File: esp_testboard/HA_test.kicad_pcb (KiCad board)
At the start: 2 copper layers, 8.3 x 5.1 mm, 90 parts, among them J1 ESP-01, J10 ESP-01, J11 SHT21, J12 SHT21, J13 SHT21, J14 SHT21, J15 SHT21, J16 PWR_IN, J17 PWR_USB, J18 UART, J2 ESP-01, J3 ESP-01, J4 ESP-01, J5 ESP-01, J6 ESP-01, J7 ESP-01, J8 ESP-01, J9 ESP-01, U1 AMS1117-3.3, U2 AMS1117-3.3

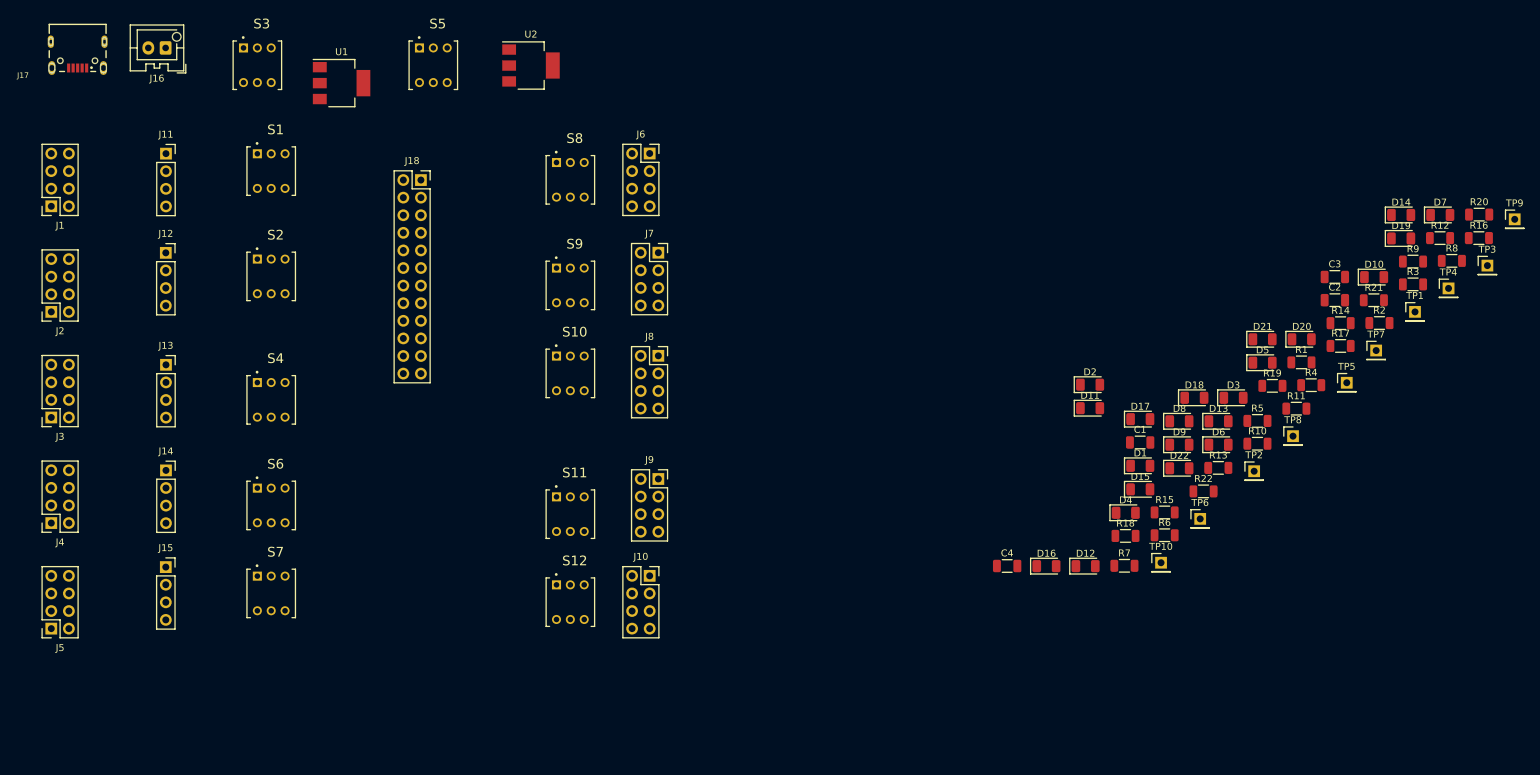
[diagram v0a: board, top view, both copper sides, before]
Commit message: schematic and PCB for ESP tester
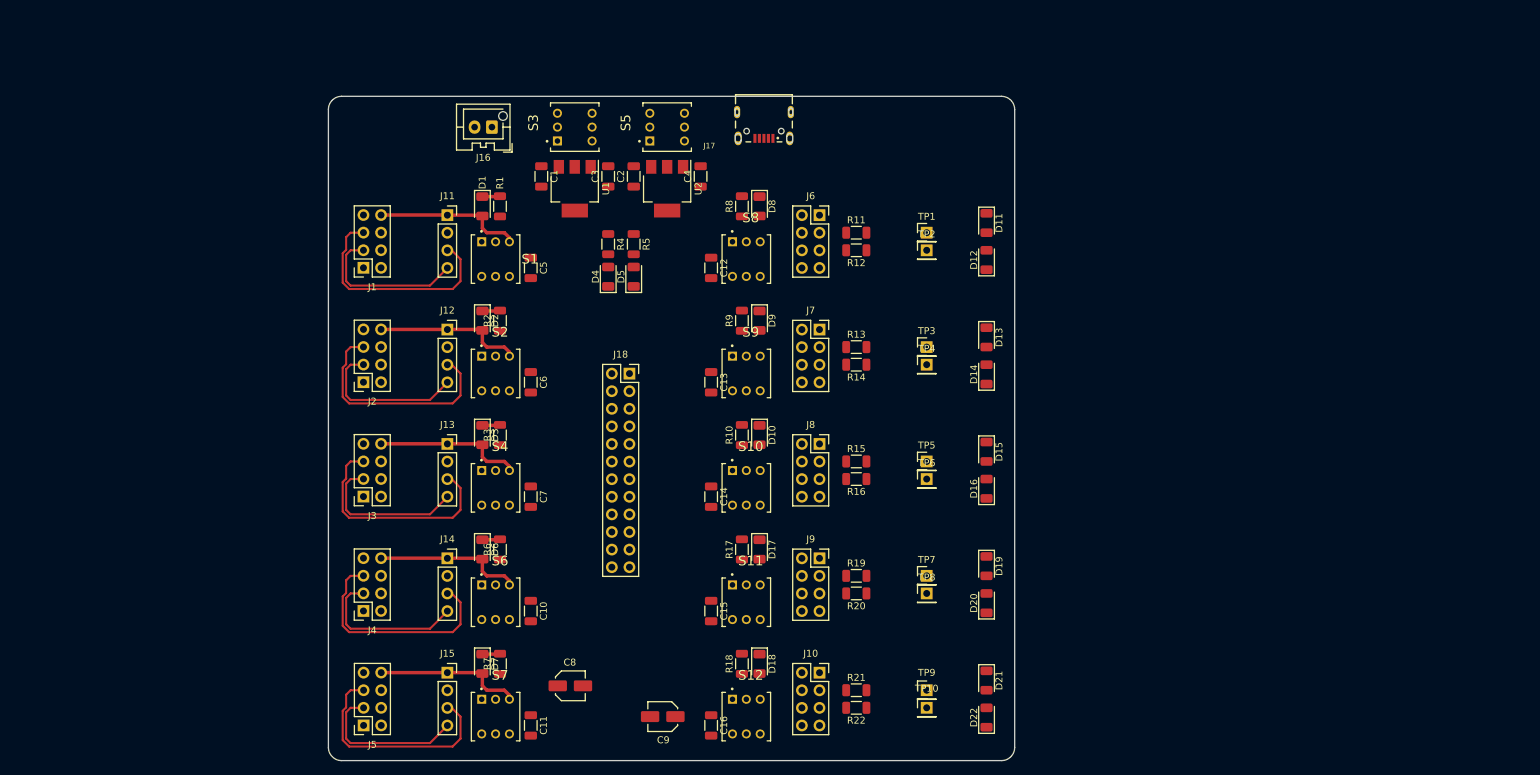
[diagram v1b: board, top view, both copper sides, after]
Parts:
- added C10: 100nF, Capacitor_SMD:C_1206_3216Metric, F.Cu at (139.1, 119.4)
- added C11: 100nF, Capacitor_SMD:C_1206_3216Metric, F.Cu at (139.1, 135.9)
- added C12: 100nF, Capacitor_SMD:C_1206_3216Metric, F.Cu at (165.1, 69.8)
- added C13: 100nF, Capacitor_SMD:C_1206_3216Metric, F.Cu at (165.1, 86.4)
- added C14: 100nF, Capacitor_SMD:C_1206_3216Metric, F.Cu at (165.1, 102.9)
- added C15: 100nF, Capacitor_SMD:C_1206_3216Metric, F.Cu at (165.1, 119.4)
- added C16: 100nF, Capacitor_SMD:C_1206_3216Metric, F.Cu at (165.1, 135.9)
- added C5: 100nF, Capacitor_SMD:C_1206_3216Metric, F.Cu at (139.1, 69.8)
- added C6: 100nF, Capacitor_SMD:C_1206_3216Metric, F.Cu at (139.1, 86.4)
- added C7: 100nF, Capacitor_SMD:C_1206_3216Metric, F.Cu at (139.1, 102.9)
- added C8: 47uF/6.3V, PJ:CAPAE430X550N, F.Cu at (144.8, 130.2)
- added C9: 47uF/6.3V, PJ:CAPAE430X550N, F.Cu at (158.1, 134.6)
- moved D7 152.7 mm to (132.1, 127.0), turned to -90 degrees
- moved R3 133.6 mm to (134.6, 94.0), turned to 90 degrees
- moved R2 127.0 mm to (134.6, 77.5), turned to 90 degrees
- moved R1 117.9 mm to (134.6, 61.0), turned to 90 degrees
- moved TP9 108.7 mm to (196.2, 130.8)
- moved D3 108.6 mm to (132.1, 94.0), turned to -90 degrees
- moved D6 107.3 mm to (132.1, 110.5), turned to -90 degrees
- moved C3 105.9 mm to (150.2, 56.6), turned to 90 degrees
- moved R20 105.2 mm to (186.1, 116.8), turned to 180 degrees
- moved R4 103.5 mm to (150.2, 66.4), turned to -90 degrees
- moved R8 102.8 mm to (169.5, 61.0), turned to 90 degrees
- moved C2 102.8 mm to (153.9, 56.6), turned to 90 degrees
- moved D1 102.1 mm to (132.1, 61.0), turned to -90 degrees
- moved J17 99.6 mm to (172.7, 48.3)
- moved R9 97.2 mm to (169.5, 77.5), turned to 90 degrees
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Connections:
- C1 pad 1: 5V -> 5VS
- C2 pad 1: 5V -> 5VC
- C4 pad 1: VCC1 -> VCC2
- R5 pad 1: VCC1 -> VCC2
- S10 pad 2: VCC1 -> VCC2
- S11 pad 2: VCC1 -> VCC2
- S12 pad 2: VCC1 -> VCC2
- S3 pad 3: 5V -> 5VS
- S5 pad 3: 5V -> 5VC
- S8 pad 2: VCC1 -> VCC2
- S9 pad 2: VCC1 -> VCC2
- U1 pad 3: 5V -> 5VS
- U2 pad 2: VCC1 -> VCC2
- U2 pad 3: 5V -> 5VC
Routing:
- net SCL4: track 0.00 -> 33.0 mm
- net SCL1: track 0.00 -> 33.0 mm
- net SCL3: track 0.00 -> 33.0 mm
- net SCL2: track 0.00 -> 33.0 mm
- net SCL5: track 0.00 -> 33.0 mm
- net SDA4: track 0.00 -> 22.5 mm
- net SDA3: track 0.00 -> 22.5 mm
- net SDA1: track 0.00 -> 22.5 mm
- net SDA5: track 0.00 -> 22.5 mm
- net SDA2: track 0.00 -> 22.5 mm
- net Net-(J11-Pad1): track 0.00 -> 21.5 mm
- net Net-(J13-Pad1): track 0.00 -> 21.3 mm
- net Net-(D6-Pad2): track 0.00 -> 21.3 mm
- net Net-(D2-Pad2): track 0.00 -> 21.3 mm
- net Net-(D7-Pad2): track 0.00 -> 21.3 mm
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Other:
- board size 8.3 x 5.1 mm -> 99.1 x 95.9 mm

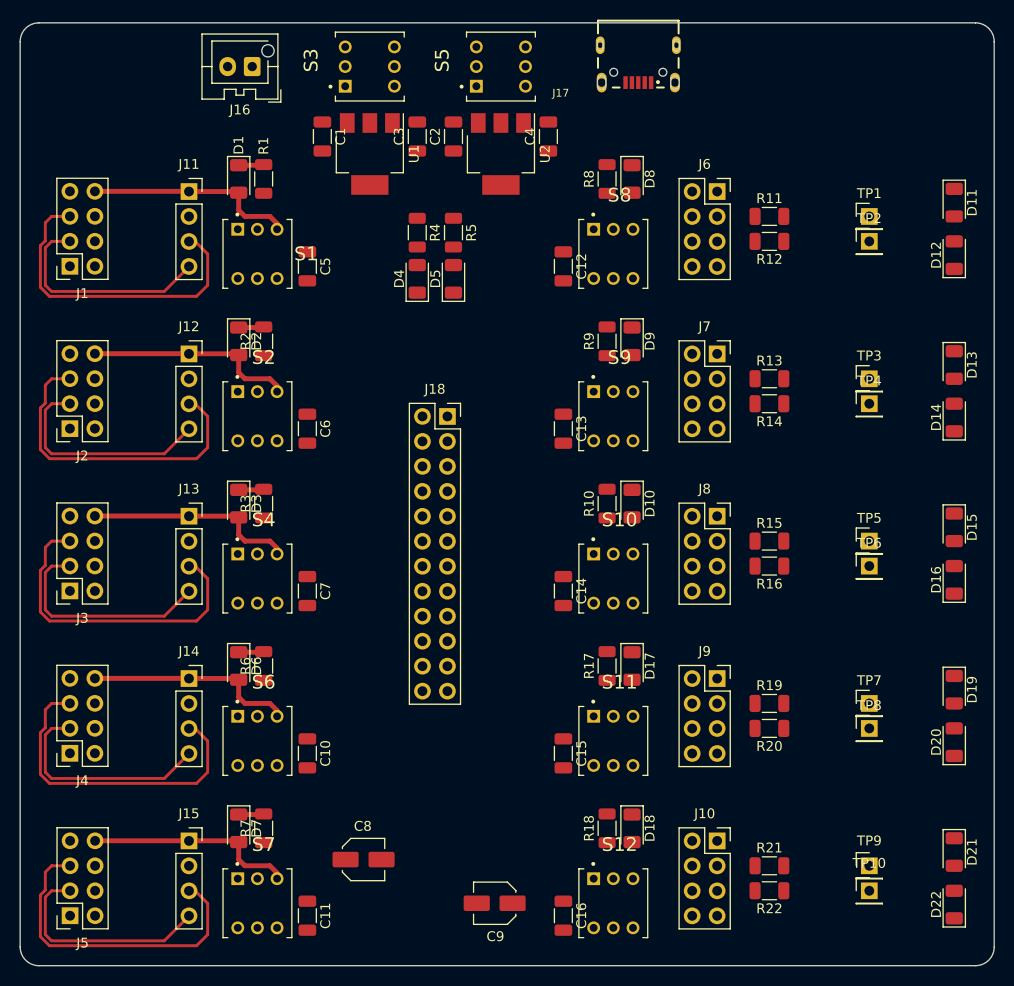
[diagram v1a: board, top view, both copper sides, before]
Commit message: Micro USB upgraded to USB-C
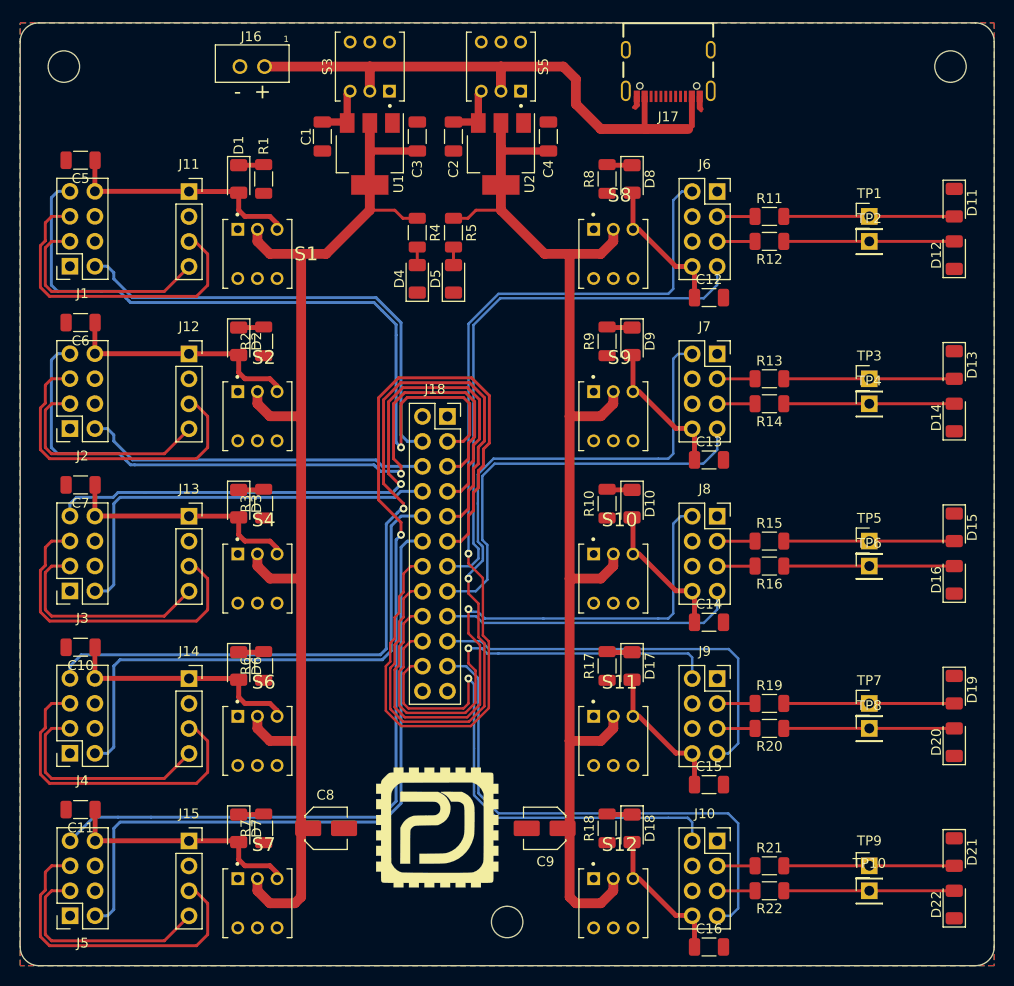
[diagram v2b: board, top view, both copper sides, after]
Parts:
- added H1: M3, MountingHole:MountingHole_3.2mm_M3, F.Cu at (204.5, 49.5)
- added H2: M3, MountingHole:MountingHole_3.2mm_M3, F.Cu at (114.3, 49.5)
- added H3: M3, MountingHole:MountingHole_3.2mm_M3, F.Cu at (159.4, 136.5)
- added Ref**: Val**, PJ:PJ_PCB, F.Cu at (152.1, 126.7)
- J16: footprint Connector_JST:JST_XA_B02B-XASK-1-A_1x02_P2.50mm_Vertical -> PJ:68800211622
- J17: value PWR_USB -> 629722000214; footprint PJ:USB_WE_629105150521 -> PJ:629722000214
- moved C10 25.5 mm to (116.0, 108.6), turned to 180 degrees
- moved C6 25.5 mm to (116.0, 75.6), turned to 180 degrees
- moved C7 25.5 mm to (116.0, 92.1), turned to 180 degrees
- moved C11 25.5 mm to (116.0, 125.1), turned to 180 degrees
- moved C5 25.5 mm to (116.0, 59.1), turned to 180 degrees
- moved C12 15.1 mm to (179.9, 73.0), turned to 0 degrees
- moved C15 15.1 mm to (179.9, 122.6), turned to 0 degrees
- moved C16 15.1 mm to (179.9, 139.1), turned to 0 degrees
- moved C13 15.1 mm to (179.9, 89.5), turned to 0 degrees
- moved C14 15.1 mm to (179.9, 106.0), turned to 0 degrees
- moved C9 9.16 mm to (163.2, 127.0)
- moved C8 4.96 mm to (141.0, 127.0)
- moved J17 3.08 mm to (175.8, 47.8)
- turned C2 to -90 degrees
- turned S3 to 180 degrees
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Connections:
- J17 pad S1: (no net) -> GND
- J17 pad S2: (no net) -> GND
- J17 pad S3: (no net) -> GND
- J17 pad S4: (no net) -> GND
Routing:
- net VCC2: track 0.00 -> 124.5 mm
- net VCC1: track 0.00 -> 124.5 mm
- net RX5: track 0.00 -> 107.2 mm, vias 0 -> 1
- net TX6: track 0.00 -> 102.4 mm, vias 0 -> 1
- net RX4: track 0.00 -> 87.2 mm, vias 0 -> 1
- net TX7: track 0.00 -> 82.4 mm, vias 0 -> 1
- net RX1: track 0.00 -> 78.1 mm, vias 0 -> 1
- net RX2: track 0.00 -> 72.8 mm, vias 0 -> 1
- net TX5: track 0.00 -> 69.2 mm
- net RX3: track 0.00 -> 66.6 mm, vias 0 -> 1
- net 5V: track 0.00 -> 66.1 mm
- net TX8: track 0.00 -> 63.7 mm, vias 0 -> 1
- net RX6: track 0.00 -> 55.8 mm
- net TX4: track 0.00 -> 55.6 mm
- net RX10: track 0.00 -> 54.1 mm
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- added copper zone on B.Cu, net GND
- added copper zone on F.Cu, net GND
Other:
- board text added: "- +"

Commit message: finished test board for ESP
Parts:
- added REF**: boardname_sticker, PJ:boardname_sticker, F.Cu at (191.8, 58.4)
- added REF**: uart_sticker, PJ:uart_sticker, F.Cu at (152.1, 77.7)
- added REF**: sensornodes_sticker, PJ:sensornodes_sticker, F.Cu at (137.9, 101.6)
- added REF**: controlnodes_sticker, PJ:controlnodes_sticker, F.Cu at (166.4, 101.6)
- added REF**: socialname_sticker, PJ:socialname_sticker, B.Cu at (152.0, 84.8)
- added Ref**: Val**, PJ:PJ_PCB, B.Cu at (152.1, 126.7)
- C1, C2, C3, C4: footprint Capacitor_SMD:C_1206_3216Metric -> Capacitor_SMD:C_0805_2012Metric
- renumbered D5 to CON_PWR, S5 to CON_SW, J1 to ESP_01, S1 to ESP_01-SW, J2 to ESP_02, S2 to ESP_02-SW, J3 to ESP_03, S4 to ESP_03-SW, J4 to ESP_04, S6 to ESP_04-SW, J5 to ESP_05, S7 to ESP_05-SW, J6 to ESP_06, S8 to ESP_06-SW, J7 to ESP_07, S9 to ESP_07-SW, J8 to ESP_08, S10 to ESP_08-SW, J9 to ESP_09, S11 to ESP_09-SW, J10 to ESP_10, S12 to ESP_10-SW, D18 to ESP_PWR, D6 to ESP_PWR, D7 to ESP_PWR, D9 to ESP_PWR, D8 to ESP_PWR, D10 to ESP_PWR, D17 to ESP_PWR, D3 to ESP_PWR, D2 to ESP_PWR, D1 to ESP_PWR, TP6 to GPIO0, TP2 to GPIO0, TP10 to GPIO0, TP4 to GPIO0, TP8 to GPIO0, TP3 to GPIO2, TP1 to GPIO2, TP5 to GPIO2, TP7 to GPIO2, TP9 to GPIO2, D11 to LED1, D15 to LED1, D13 to LED1, D21 to LED1, D19 to LED1, D16 to LED2, D12 to LED2, D22 to LED2, D20 to LED2, D14 to LED2, J16 to PWR_CON, D4 to SEN_PWR, S3 to SEN_SW, J11 to SHT21, J12 to SHT21, J13 to SHT21, J14 to SHT21, J15 to SHT21, J17 to USB
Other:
- board text added: "3V3 GND SCL SDA"
- board text added: "GND RX1 RX2 RX3 RX4 RX5 RX6 RX7 RX8 RX9 RX10 GND"
- board text added: "GND TX1 TX2 TX3 TX4 TX5 TX6 TX7 TX8 TX9 TX10 GND"
- board text added: "paweljagowdzik@gmail.com"
